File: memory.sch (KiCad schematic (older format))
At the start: 23 parts, among them J6 Conn_01x03, U11 74HC00, U12 4164, U13 4164, U14 4164, U15 4164, U16 28C256, U17 4164, U18 4164, U19 4164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

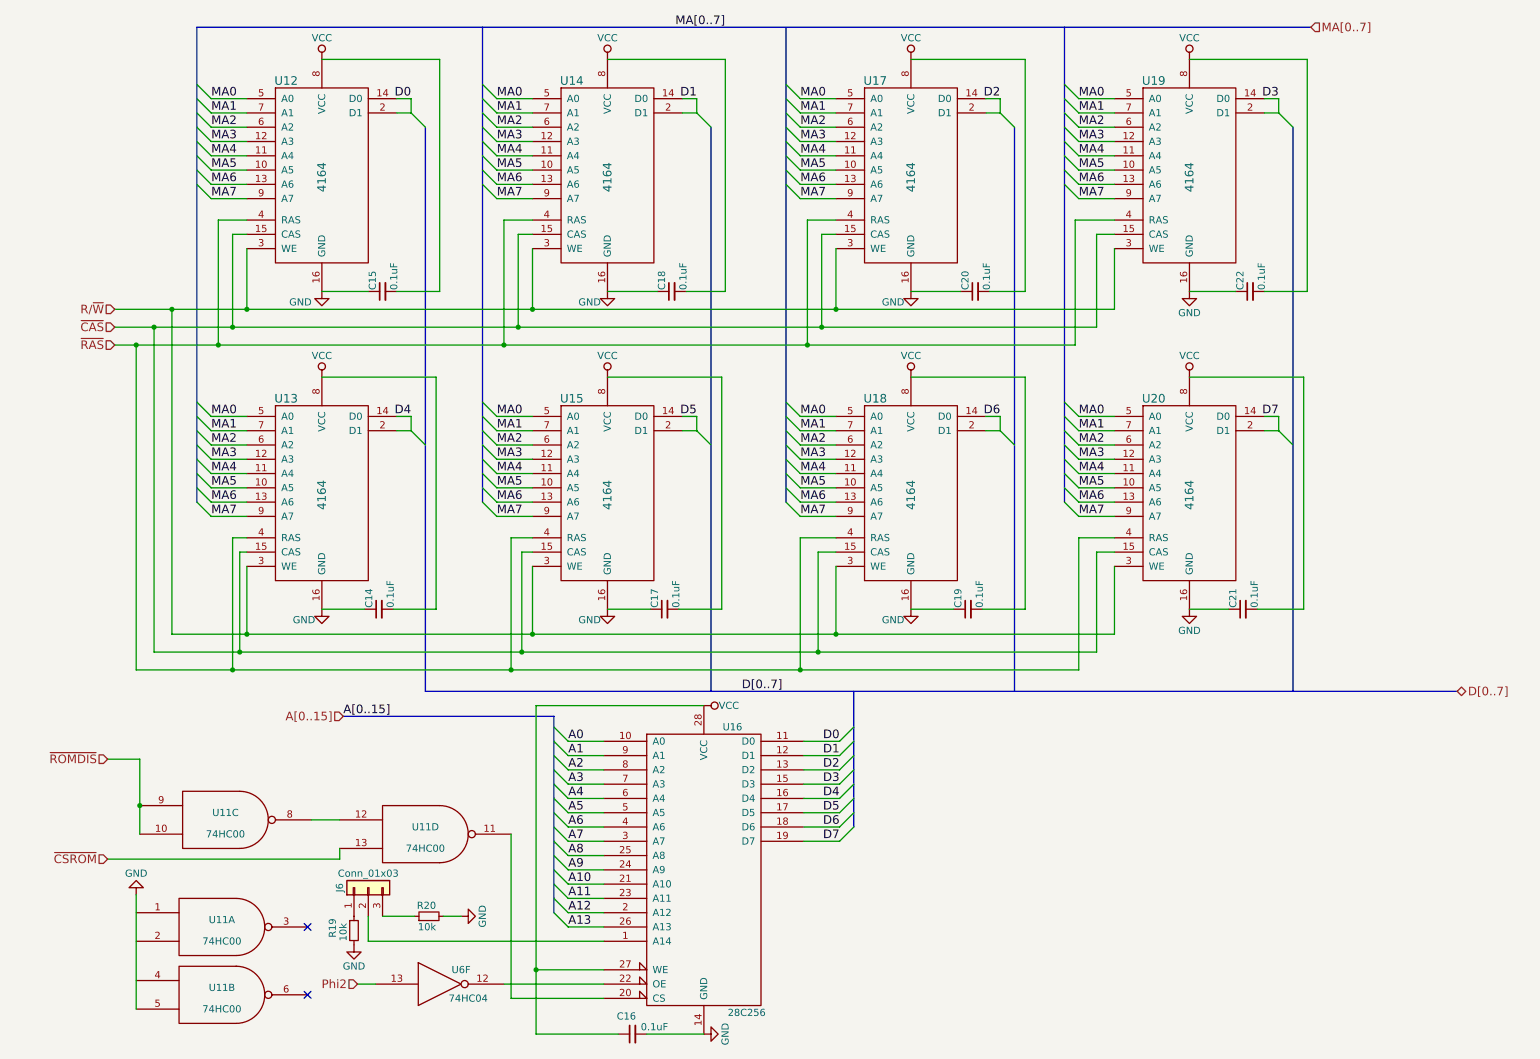
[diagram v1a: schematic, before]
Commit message: Added some comments and equs
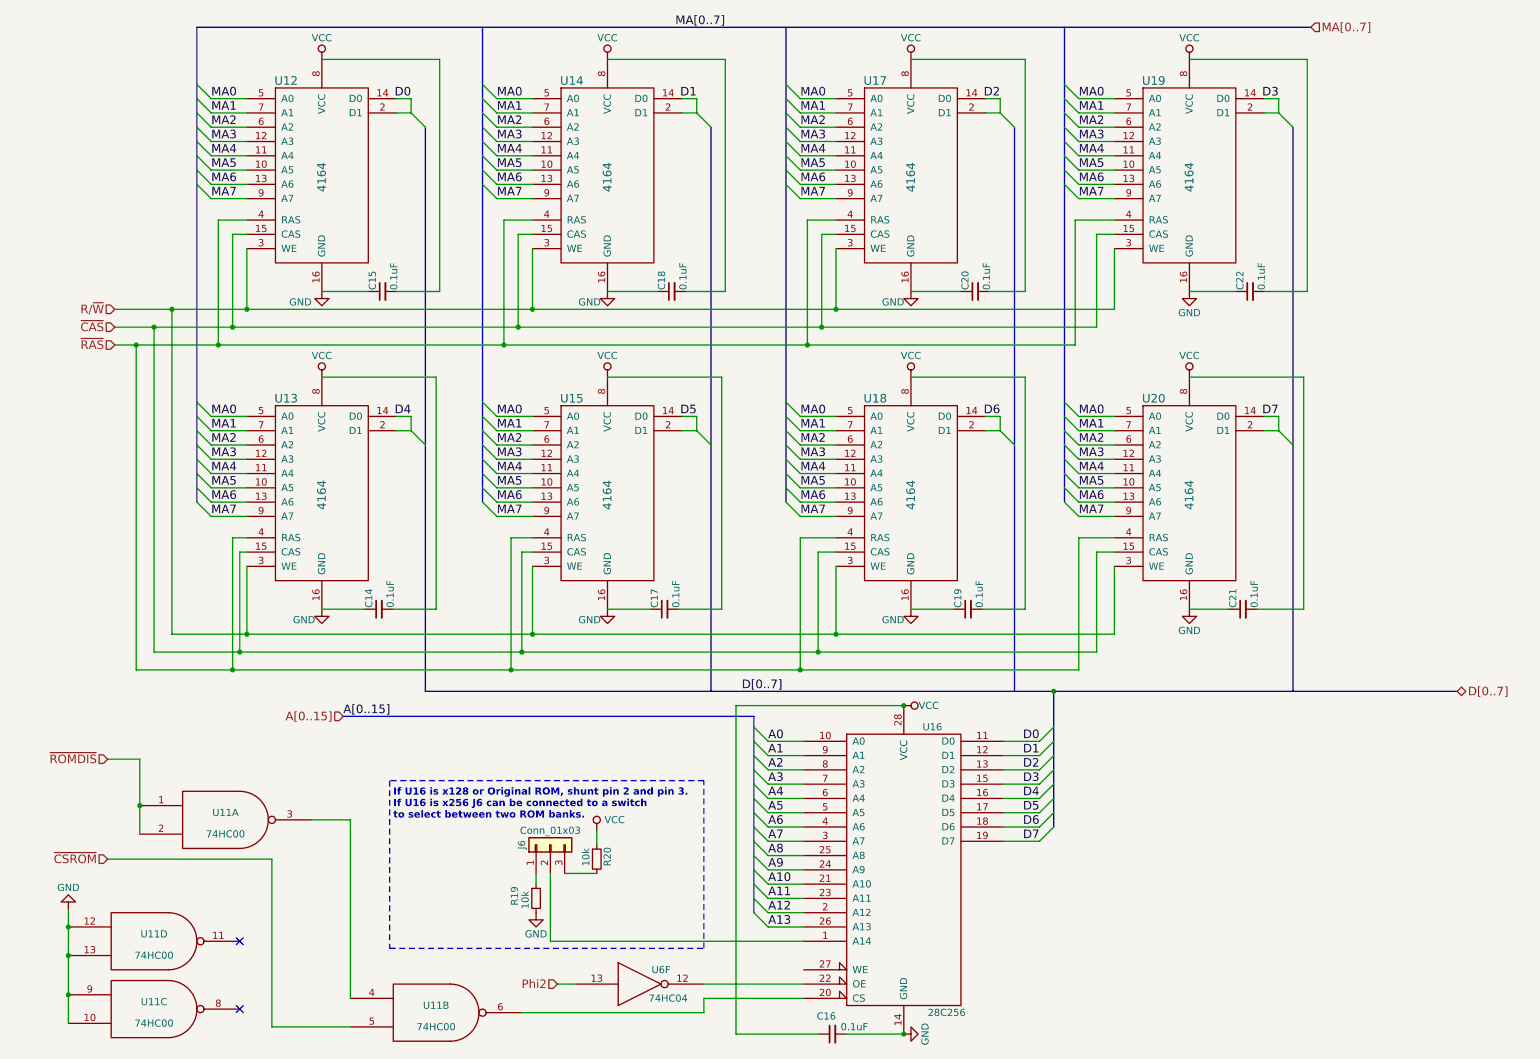
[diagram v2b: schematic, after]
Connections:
- net GND: now also U11.10, U11.12, U11.13, U11.9; no longer R20.2, U11.5
- net VCC: now also R20.1; no longer U16.27 (WE)
- net ~CSROM: now also U11.5; no longer U11.13
- net ~ROMDIS: now also U11.1, U11.2; no longer U11.10, U11.9
- net at U11.8: no longer U11.12
- net at U11.11: no longer U16.20 (CS)
- net at U11.3: now also U11.4
- net at U11.6: now also U16.20 (CS)
- net at J6.3 (Pin_3): now also R20.2; no longer R20.1
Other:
- note added: "If U16 is x128 or Original ROM, shunt pin 2 and pin 3.\nIf U16 is x256 J6 can be connected to a switch \nto select between two ROM banks."
- moved on the sheet: C16, J6, R19, R20, U11A, U11B, U11C, U11D, U16, U6F
